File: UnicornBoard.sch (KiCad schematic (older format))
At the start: 37 parts, among them J2 USB_B_Micro, J4 Conn_01x01, J5 Conn_01x01, J6 Conn_01x01, J7 Conn_01x01, SW1 SW_Push, U1 ATSAMD21E18A-AU, U2 AP2112K-3.3

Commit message: Candy the Catacorn
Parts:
- added BT1: Battery, Connector_JST:JST_PH_S2B-PH-SM4-TB_1x02-1MP_P2.00mm_Horizontal, symbol Device:Battery
- added D50: D_Schottky, Diode_SMD:D_SOD-123F, symbol Device:D_Schottky
- added H1, H2: MountingHole, MountingHole:MountingHole_2.2mm_M2_ISO7380_Pad, symbol Mechanical:MountingHole
- C1: renamed from C5; value C -> 1 uF C
- C2: renamed from C6; value C -> 10 uF C
- C3: renamed from C7; value C -> 10 uF C
- C4: renamed from C8; value C -> 1 uF C
- D4: renamed from Tail0; footprint LED_SMD:LED_0402_1005Metric -> LED_SMD:LED_0805_2012Metric_Pad1.15x1.40mm_HandSolder
- D5: renamed from Tail2; footprint LED_SMD:LED_0402_1005Metric -> LED_SMD:LED_0805_2012Metric_Pad1.15x1.40mm_HandSolder
- D51: renamed from D7; footprint Diode_SMD:D_SOT-23_ANK -> Diode_SMD:D_SOD-123F
- D6: renamed from Tail1; footprint LED_SMD:LED_0402_1005Metric -> LED_SMD:LED_0805_2012Metric_Pad1.15x1.40mm_HandSolder
- D7: renamed from D6; footprint LED_SMD:LED_0402_1005Metric -> LED_SMD:LED_0805_2012Metric_Pad1.15x1.40mm_HandSolder
- D8: renamed from D1; footprint LED_SMD:LED_0402_1005Metric -> LED_SMD:LED_0805_2012Metric_Pad1.15x1.40mm_HandSolder
- D9: renamed from D2; footprint LED_SMD:LED_0402_1005Metric -> LED_SMD:LED_0805_2012Metric_Pad1.15x1.40mm_HandSolder
- R0: renamed from R1; value R -> 180R
- R1: renamed from R3; value R -> 180R
- R2: renamed from R4; value R -> 30R; footprint Resistor_SMD:R_0805_2012Metric_Pad1.15x1.40mm_HandSolder -> Resistor_SMD:R_1206_3216Metric_Pad1.42x1.75mm_HandSolder
- R3: renamed from R5; value R -> 30R; footprint Resistor_SMD:R_0805_2012Metric_Pad1.15x1.40mm_HandSolder -> Resistor_SMD:R_1206_3216Metric_Pad1.42x1.75mm_HandSolder
- R4: renamed from R6; value R -> 100R; footprint Resistor_SMD:R_0402_1005Metric -> Resistor_SMD:R_0603_1608Metric_Pad1.05x0.95mm_HandSolder
- R5: renamed from R7; value R -> 100R; footprint Resistor_SMD:R_0402_1005Metric -> Resistor_SMD:R_0603_1608Metric_Pad1.05x0.95mm_HandSolder
- R6: renamed from R8; value R -> 100R; footprint Resistor_SMD:R_0402_1005Metric -> Resistor_SMD:R_0603_1608Metric_Pad1.05x0.95mm_HandSolder
- R7: renamed from R2; value R -> 330R; footprint Resistor_SMD:R_0402_1005Metric -> Resistor_SMD:R_0805_2012Metric_Pad1.15x1.40mm_HandSolder
- R8: renamed from R9; value R -> 330R; footprint Resistor_SMD:R_0402_1005Metric -> Resistor_SMD:R_0805_2012Metric_Pad1.15x1.40mm_HandSolder
- R9: renamed from R10; value R -> 330R; footprint Resistor_SMD:R_0402_1005Metric -> Resistor_SMD:R_0805_2012Metric_Pad1.15x1.40mm_HandSolder
- renumbered J6 to 3V3, D5 to D0, D3 to D1, Paw0 to D2, Paw1 to D3, Dot0 to Dot2, J7 to GND1, J4 to J31, J5 to J32, J2 to J5, Touch2 to Touch1, Touch1 to Touch2
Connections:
- net +3V3: now also C2.2, R8.1, R9.1; no longer C2.1
- net GND: now also C2.1, BT1.2 (-); no longer C2.2
- net at C3.1, D51.1 (K), U2.1 (VIN)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: now also D50.1 (K)
- net at R0.1, U1.13 (PA10): now also R1.1; no longer R1.2
- net at D7.2 (A), R7.2: no longer R8.1, R9.1
- net at D1.2 (A): now also R1.2; no longer R1.1
- new net +BATT: BT1.1 (+), D50.2 (A)
- no-connect marks 0 -> 20
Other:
- moved on the sheet: 3V3, C2, C3, C4, D51, D7, D8, D9, GND1, J31, J32, R1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

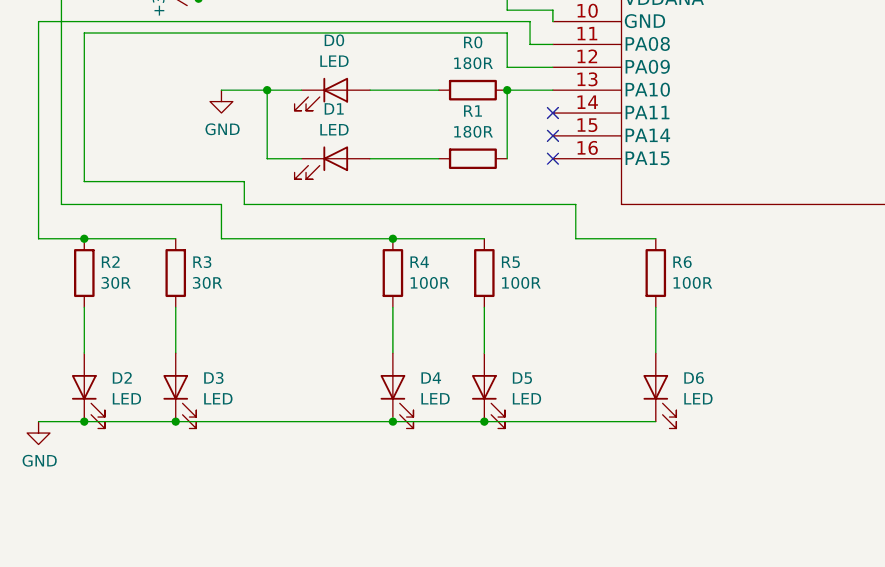
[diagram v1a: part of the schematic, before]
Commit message: Added BOM and tweaked resistor values to keep current in spec for GPIO pins
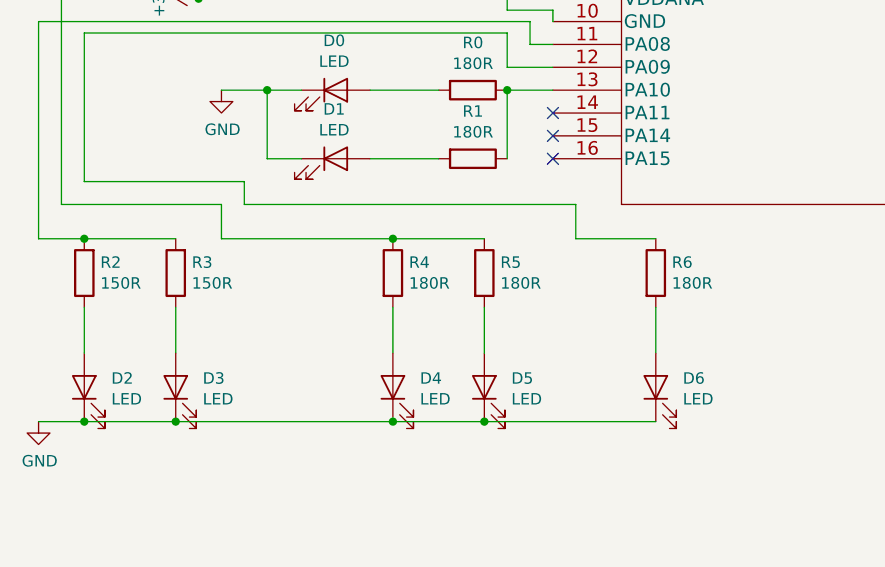
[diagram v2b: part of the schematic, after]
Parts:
- R2, R3: value 30R -> 150R
- R4, R5, R6: value 100R -> 180R
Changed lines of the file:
@@
 P 750 4300
 F 0 "R2" H 680 4254 50  0000 R CNN
-F 1 "30R" H 680 4345 50  0000 R CNN
+F 1 "150R" H 680 4345 50  0000 R CNN
 F 2 "Resistor_SMD:R_1206_3216Metric_Pad1.42x1.75mm_HandSolder" V 680 4300 50  0001 C CNN
 F 3 "~" H 750 4300 50  0001 C CNN
@@
 P 1150 4300
 F 0 "R3" H 1080 4254 50  0000 R CNN
-F 1 "30R" H 1080 4345 50  0000 R CNN
+F 1 "150R" H 1080 4345 50  0000 R CNN
 F 2 "Resistor_SMD:R_1206_3216Metric_Pad1.42x1.75mm_HandSolder" V 1080 4300 50  0001 C CNN
 F 3 "~" H 1150 4300 50  0001 C CNN
@@
 P 2100 4300
 F 0 "R4" H 2170 4346 50  0000 L CNN
-F 1 "100R" H 2170 4255 50  0000 L CNN
+F 1 "180R" H 2170 4255 50  0000 L CNN
 F 2 "Resistor_SMD:R_0603_1608Metric_Pad1.05x0.95mm_HandSolder" V 2030 4300 50  0001 C CNN
 F 3 "~" H 2100 4300 50  0001 C CNN
@@
 P 2500 4300
 F 0 "R5" H 2570 4346 50  0000 L CNN
-F 1 "100R" H 2570 4255 50  0000 L CNN
+F 1 "180R" H 2570 4255 50  0000 L CNN
 F 2 "Resistor_SMD:R_0603_1608Metric_Pad1.05x0.95mm_HandSolder" V 2430 4300 50  0001 C CNN
 F 3 "~" H 2500 4300 50  0001 C CNN
@@
 P 3250 4300
 F 0 "R6" H 3320 4346 50  0000 L CNN
-F 1 "100R" H 3320 4255 50  0000 L CNN
+F 1 "180R" H 3320 4255 50  0000 L CNN
 F 2 "Resistor_SMD:R_0603_1608Metric_Pad1.05x0.95mm_HandSolder" V 3180 4300 50  0001 C CNN
 F 3 "~" H 3250 4300 50  0001 C CNN
